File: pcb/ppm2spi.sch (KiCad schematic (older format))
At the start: 38 parts, among them IC1 ATMEGA328-A, K1 CONN_3, P1 CONN_5, P2 CONN_6, P3 CONN_3X2, P4 CONN_6, SW1 SW_PUSH, U1 MCP1702-5v, U2 MCP1702-3.3v, X1 16Mhz

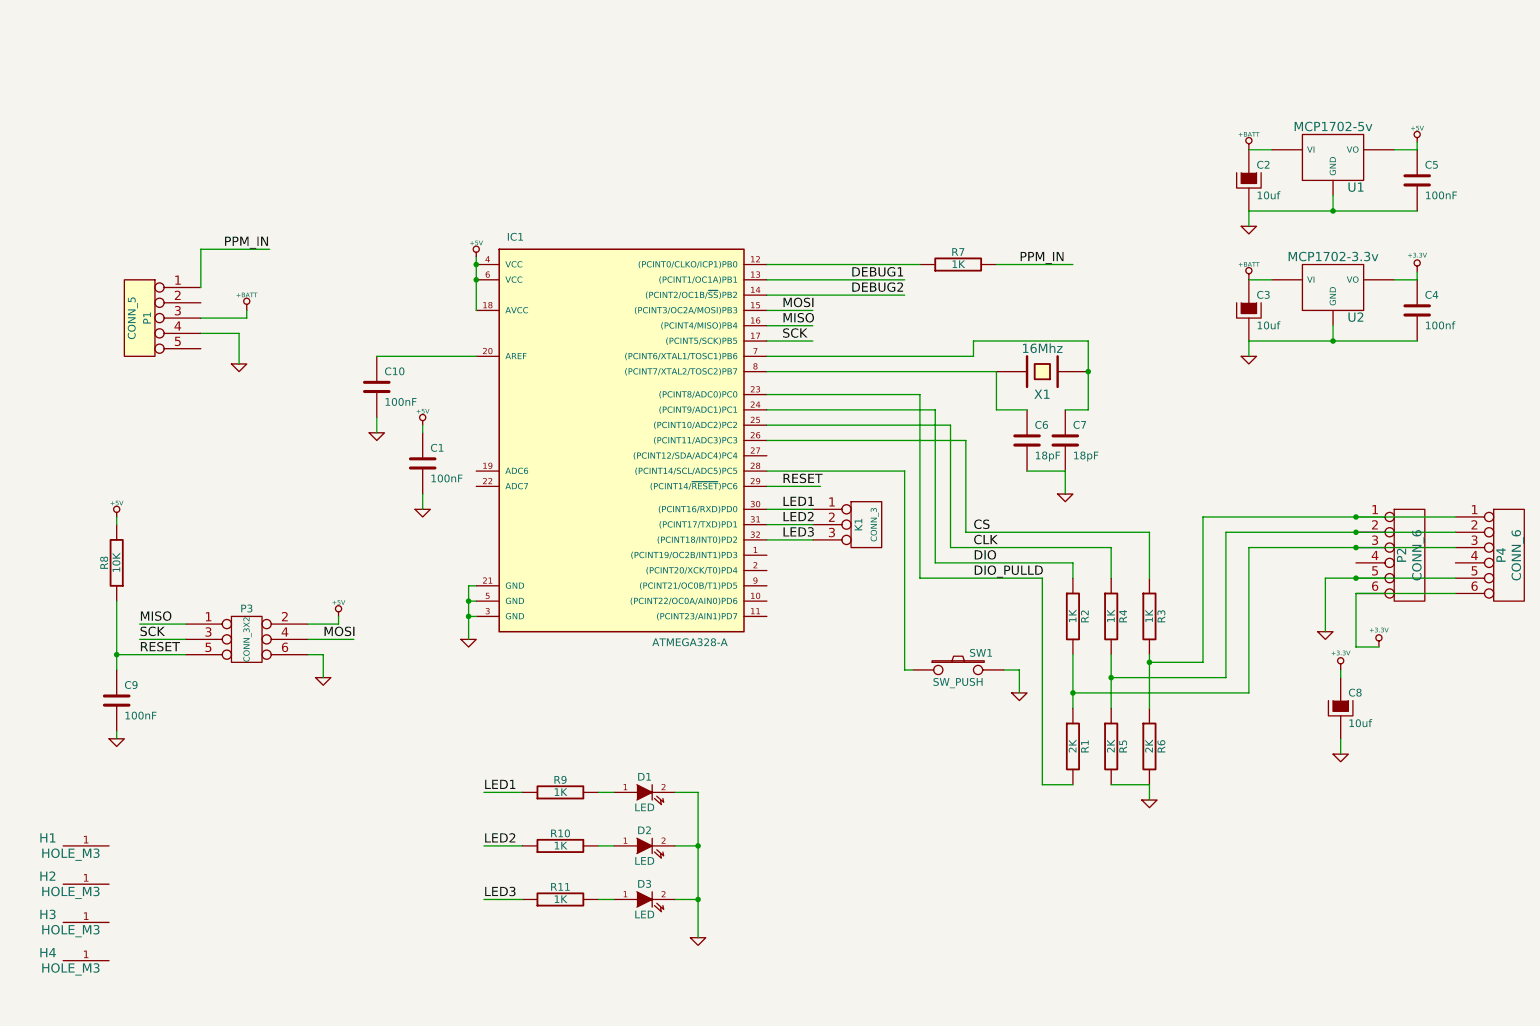
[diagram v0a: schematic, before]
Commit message: Hardware changes to allow a serial input as well as PPM
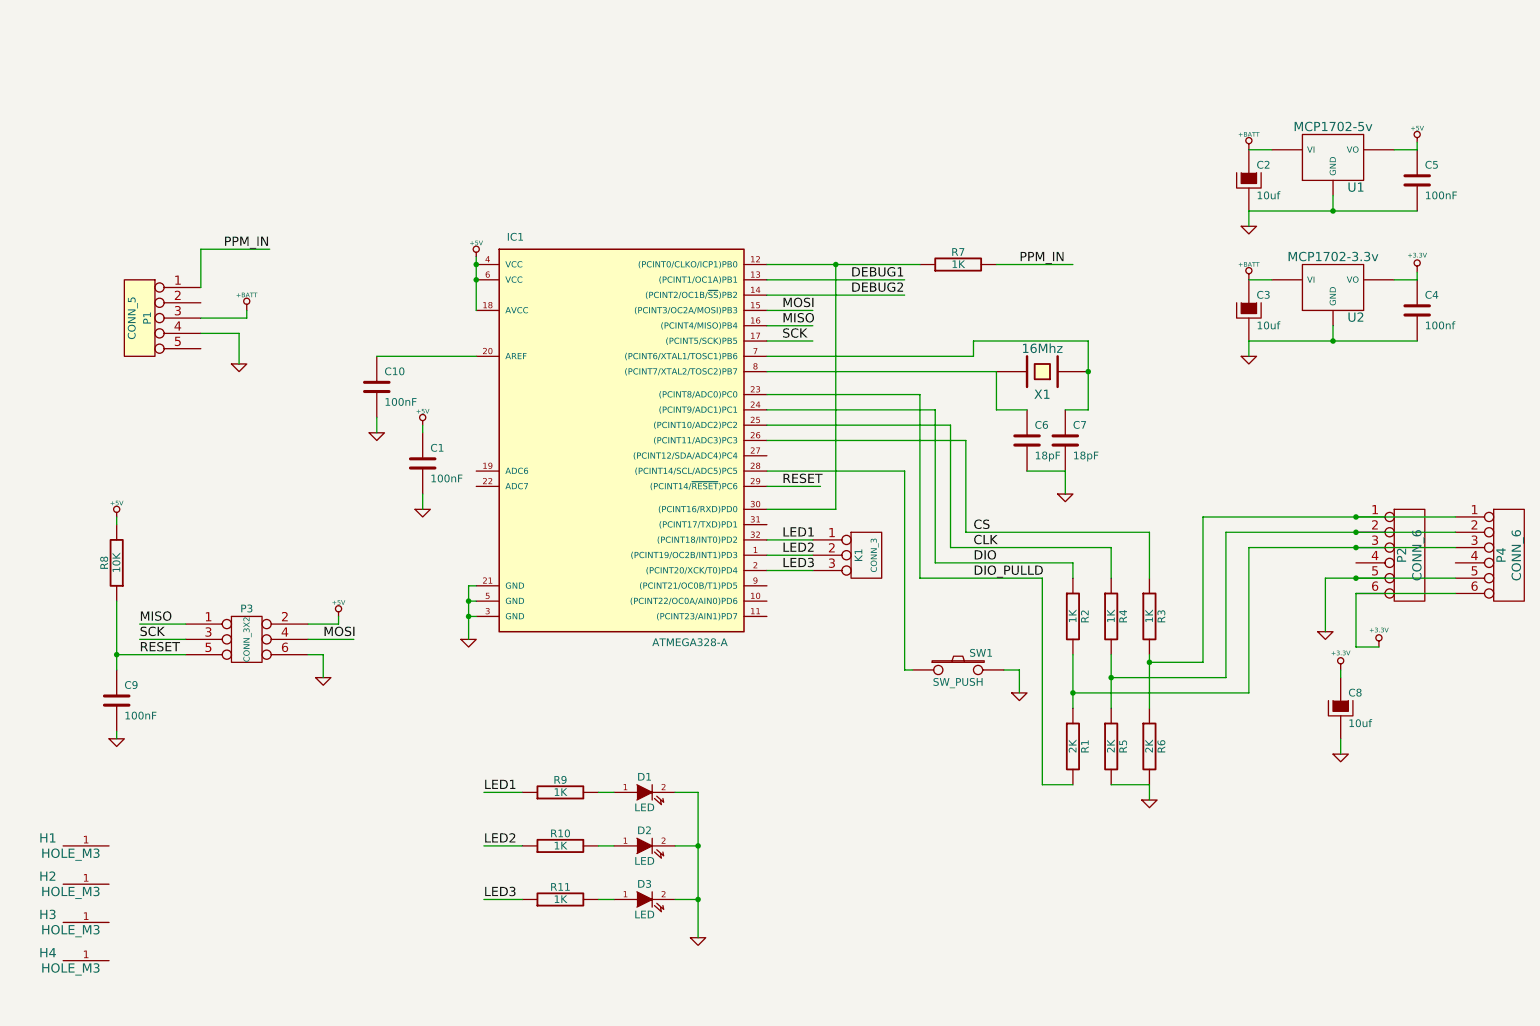
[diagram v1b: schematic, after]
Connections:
- wire segments 112 -> 114
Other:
- moved on the sheet: K1

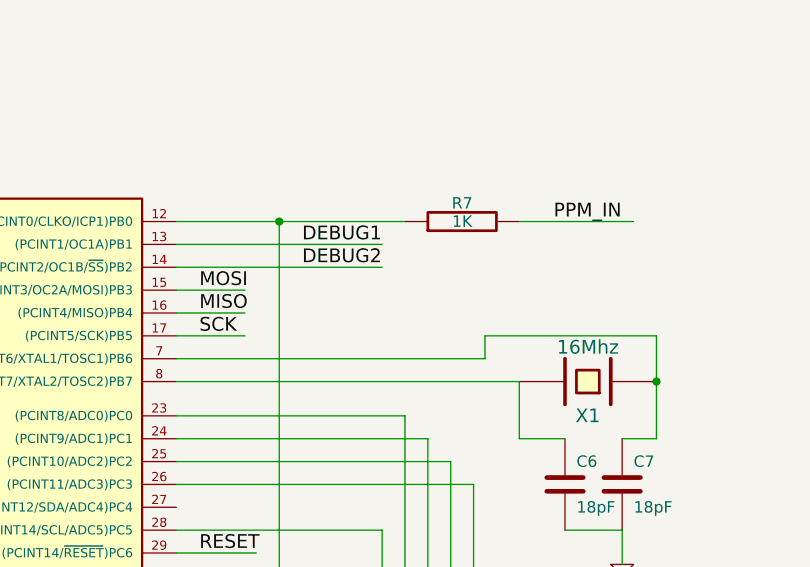
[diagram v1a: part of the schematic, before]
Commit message: Forgot to break out the debug pins
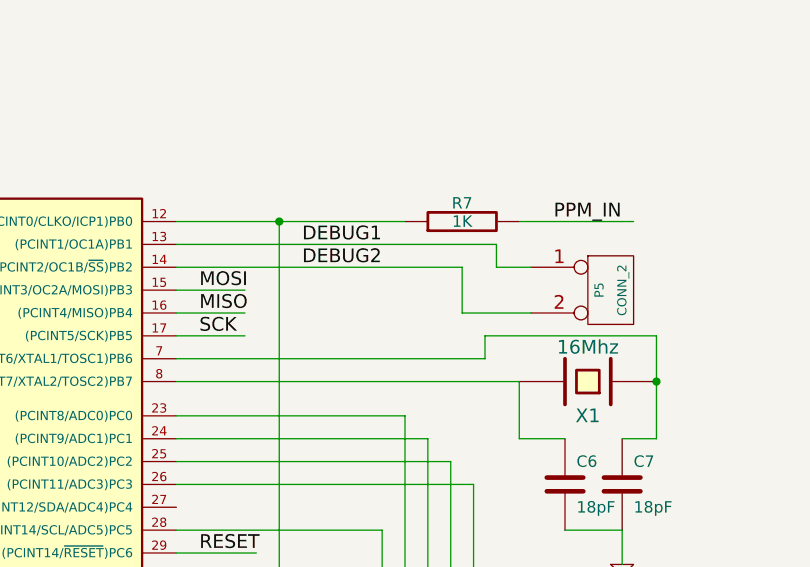
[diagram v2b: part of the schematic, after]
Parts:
- added P5: CONN_2, symbol CONN_2
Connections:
- wire segments 114 -> 118
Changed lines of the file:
@@
-EESchema Schematic File Version 2  date 14/03/2013 13:46:19
+EESchema Schematic File Version 2  date 14/03/2013 13:59:10
 LIBS:power
 LIBS:device
@@
 Comment4 ""
 $EndDescr
+Wire Wire Line
+	7450 2800 7150 2800
+Wire Wire Line
+	7150 2800 7150 2600
+Wire Wire Line
+	7150 2600 5900 2600
 Connection ~ 6350 2400
 Wire Wire Line
@@
 Wire Wire Line
 	5900 3850 6250 3850
-Wire Wire Line
-	6800 2500 5900 2500
 Wire Wire Line
 	5900 3750 6800 3750
@@
 	7400 3100 5900 3100
 Wire Wire Line
-	6800 2600 5900 2600
-Wire Wire Line
 	6900 2400 5900 2400
 Wire Wire Line
@@
 Wire Wire Line
 	6200 4400 5900 4400
+Wire Wire Line
+	5900 2500 7300 2500
+Wire Wire Line
+	7300 2500 7300 2600
+Wire Wire Line
+	7300 2600 7450 2600
+$Comp
+L CONN_2 P5
+U 1 1 5141D78A
+P 7800 2700
+F 0 "P5" V 7750 2700 40  0000 C CNN
+F 1 "CONN_2" V 7850 2700 40  0000 C CNN
+	1    7800 2700
+	1    0    0    -1
+$EndComp
 $Comp
 L CONN_6 P4
@@
 LED1
 $Comp
-L GND #PWR7
+L GND #PWR01
 U 1 1 513E082D
 P 3350 3500
-F 0 "#PWR7" H 3350 3500 30  0001 C CNN
+F 0 "#PWR01" H 3350 3500 30  0001 C CNN
 F 1 "GND" H 3350 3430 30  0001 C CNN
 	1    3350 3500
@@
 $EndComp
 $Comp
-L GND #PWR2
+L GND #PWR02
 U 1 1 513E07C2
 P 1650 5500
-F 0 "#PWR2" H 1650 5500 30  0001 C CNN
+F 0 "#PWR02" H 1650 5500 30  0001 C CNN
 F 1 "GND" H 1650 5430 30  0001 C CNN
 	1    1650 5500
@@
 $EndComp
 $Comp
-L +5V #PWR1
+L +5V #PWR03
 U 1 1 513E07BE
 P 1650 4050
-F 0 "#PWR1" H 1650 4140 20  0001 C CNN
+F 0 "#PWR03" H 1650 4140 20  0001 C CNN
 F 1 "+5V" H 1650 4140 30  0000 C CNN
 	1    1650 4050
@@
 $EndComp
 $Comp
-L +5V #PWR6
+L +5V #PWR04
 U 1 1 513E06E3
 P 3100 4700
-F 0 "#PWR6" H 3100 4790 20  0001 C CNN
+F 0 "#PWR04" H 3100 4790 20  0001 C CNN
 F 1 "+5V" H 3100 4790 30  0000 C CNN
 	1    3100 4700
@@
 $EndComp
 $Comp
-L GND #PWR5
+L GND #PWR05
 U 1 1 513E06E0
 P 3000 5100
-F 0 "#PWR5" H 3000 5100 30  0001 C CNN
+F 0 "#PWR05" H 3000 5100 30  0001 C CNN
 F 1 "GND" H 3000 5030 30  0001 C CNN
 	1    3000 5100
@@
 LED1
 $Comp
-L GND #PWR12
+L GND #PWR06
 U 1 1 513E05CD
 P 5450 6800
-F 0 "#PWR12" H 5450 6800 30  0001 C CNN
+F 0 "#PWR06" H 5450 6800 30  0001 C CNN
 F 1 "GND" H 5450 6730 30  0001 C CNN
 	1    5450 6800
@@
 $EndComp
 $Comp
-L GND #PWR9
+L GND #PWR07
 U 1 1 513E05A6
 P 3650 4000
-F 0 "#PWR9" H 3650 4000 30  0001 C CNN
+F 0 "#PWR07" H 3650 4000 30  0001 C CNN
 F 1 "GND" H 3650 3930 30  0001 C CNN
 	1    3650 4000
@@
 $EndComp
 $Comp
-L +5V #PWR8
+L +5V #PWR08
 U 1 1 513E05A3
 P 3650 3450
-F 0 "#PWR8" H 3650 3540 20  0001 C CNN
+F 0 "#PWR08" H 3650 3540 20  0001 C CNN
 F 1 "+5V" H 3650 3540 30  0000 C CNN
 	1    3650 3450
@@
 PPM_IN
 $Comp
-L GND #PWR13
+L GND #PWR09
 U 1 1 513E054D
 P 7550 5200
-F 0 "#PWR13" H 7550 5200 30  0001 C CNN
+F 0 "#PWR09" H 7550 5200 30  0001 C CNN
 F 1 "GND" H 7550 5130 30  0001 C CNN
 	1    7550 5200
@@
 $EndComp
 $Comp
-L +3.3V #PWR21
+L +3.3V #PWR010
 U 1 1 513E04F8
 P 9650 5050
-F 0 "#PWR21" H 9650 5010 30  0001 C CNN
+F 0 "#PWR010" H 9650 5010 30  0001 C CNN
 F 1 "+3.3V" H 9650 5160 30  0000 C CNN
 	1    9650 5050
@@
 $EndComp
 $Comp
-L GND #PWR22
+L GND #PWR011
 U 1 1 513E04F3
 P 9650 5600
-F 0 "#PWR22" H 9650 5600 30  0001 C CNN
+F 0 "#PWR011" H 9650 5600 30  0001 C CNN
 F 1 "GND" H 9650 5530 30  0001 C CNN
 	1    9650 5600
@@
 $EndComp
 $Comp
-L +3.3V #PWR23
+L +3.3V #PWR012
 U 1 1 513E04BE
 P 9900 4900
-F 0 "#PWR23" H 9900 4860 30  0001 C CNN
+F 0 "#PWR012" H 9900 4860 30  0001 C CNN
 F 1 "+3.3V" H 9900 5010 30  0000 C CNN
 	1    9900 4900
@@
 $EndComp
 $Comp
-L GND #PWR20
+L GND #PWR013
 U 1 1 513E04B0
 P 9550 4800
-F 0 "#PWR20" H 9550 4800 30  0001 C CNN
+F 0 "#PWR013" H 9550 4800 30  0001 C CNN
 F 1 "GND" H 9550 4730 30  0001 C CNN
 	1    9550 4800
@@
 $EndComp
 $Comp
-L +5V #PWR11
+L +5V #PWR014
 U 1 1 513E045A
 P 4000 2350
-F 0 "#PWR11" H 4000 2440 20  0001 C CNN
+F 0 "#PWR014" H 4000 2440 20  0001 C CNN
 F 1 "+5V" H 4000 2440 30  0000 C CNN
 	1    4000 2350
@@
 $EndComp
 $Comp
-L GND #PWR10
+L GND #PWR015
 U 1 1 513E0448
 P 3950 4850
-F 0 "#PWR10" H 3950 4850 30  0001 C CNN
+F 0 "#PWR015" H 3950 4850 30  0001 C CNN
 F 1 "GND" H 3950 4780 30  0001 C CNN
 	1    3950 4850
@@
 CS
 $Comp
-L GND #PWR15
+L GND #PWR016
 U 1 1 513E0385
 P 8400 5900
-F 0 "#PWR15" H 8400 5900 30  0001 C CNN
+F 0 "#PWR016" H 8400 5900 30  0001 C CNN
 F 1 "GND" H 8400 5830 30  0001 C CNN
 	1    8400 5900
@@
 $EndComp
 $Comp
-L +3.3V #PWR25
+L +3.3V #PWR017
 U 1 1 513E027A
 P 10150 2450
-F 0 "#PWR25" H 10150 2410 30  0001 C CNN
+F 0 "#PWR017" H 10150 2410 30  0001 C CNN
 F 1 "+3.3V" H 10150 2560 30  0000 C CNN
 	1    10150 2450
@@
 $EndComp
 $Comp
-L +5V #PWR24
+L +5V #PWR018
 U 1 1 513E0273
 P 10150 1600
-F 0 "#PWR24" H 10150 1690 20  0001 C CNN
+F 0 "#PWR018" H 10150 1690 20  0001 C CNN
 F 1 "+5V" H 10150 1690 30  0000 C CNN
 	1    10150 1600
@@
 $EndComp
 $Comp
-L +BATT #PWR4
+L +BATT #PWR019
 U 1 1 513E01EB
 P 2500 2700
-F 0 "#PWR4" H 2500 2650 20  0001 C CNN
+F 0 "#PWR019" H 2500 2650 20  0001 C CNN
 F 1 "+BATT" H 2500 2800 30  0000 C CNN
 	1    2500 2700
@@
 $EndComp
 $Comp
-L +BATT #PWR18
+L +BATT #PWR020
 U 1 1 513E01E7
 P 9050 2500
-F 0 "#PWR18" H 9050 2450 20  0001 C CNN
+F 0 "#PWR020" H 9050 2450 20  0001 C CNN
 F 1 "+BATT" H 9050 2600 30  0000 C CNN
 	1    9050 2500
@@
 $EndComp
 $Comp
-L +BATT #PWR16
+L +BATT #PWR021
 U 1 1 513E01E0
 P 9050 1650
-F 0 "#PWR16" H 9050 1600 20  0001 C CNN
+F 0 "#PWR021" H 9050 1600 20  0001 C CNN
 F 1 "+BATT" H 9050 1750 30  0000 C CNN
 	1    9050 1650
@@
 PPM_IN
 $Comp
-L GND #PWR3
+L GND #PWR022
 U 1 1 513E01B7
 P 2450 3050
-F 0 "#PWR3" H 2450 3050 30  0001 C CNN
+F 0 "#PWR022" H 2450 3050 30  0001 C CNN
 F 1 "GND" H 2450 2980 30  0001 C CNN
 	1    2450 3050
@@
 $EndComp
 $Comp
-L GND #PWR17
+L GND #PWR023
 U 1 1 513E019B
 P 9050 2150
-F 0 "#PWR17" H 9050 2150 30  0001 C CNN
+F 0 "#PWR023" H 9050 2150 30  0001 C CNN
 F 1 "GND" H 9050 2080 30  0001 C CNN
 	1    9050 2150
@@
 $EndComp
 $Comp
-L GND #PWR19
+L GND #PWR024
 U 1 1 513E0198
 P 9050 3000
-F 0 "#PWR19" H 9050 3000 30  0001 C CNN
+F 0 "#PWR024" H 9050 3000 30  0001 C CNN
 F 1 "GND" H 9050 2930 30  0001 C CNN
 	1    9050 3000
@@
 $EndComp
 $Comp
-L GND #PWR14
+L GND #PWR025
 U 1 1 513E0151
 P 7850 3900
-F 0 "#PWR14" H 7850 3900 30  0001 C CNN
+F 0 "#PWR025" H 7850 3900 30  0001 C CNN
 F 1 "GND" H 7850 3830 30  0001 C CNN
 	1    7850 3900

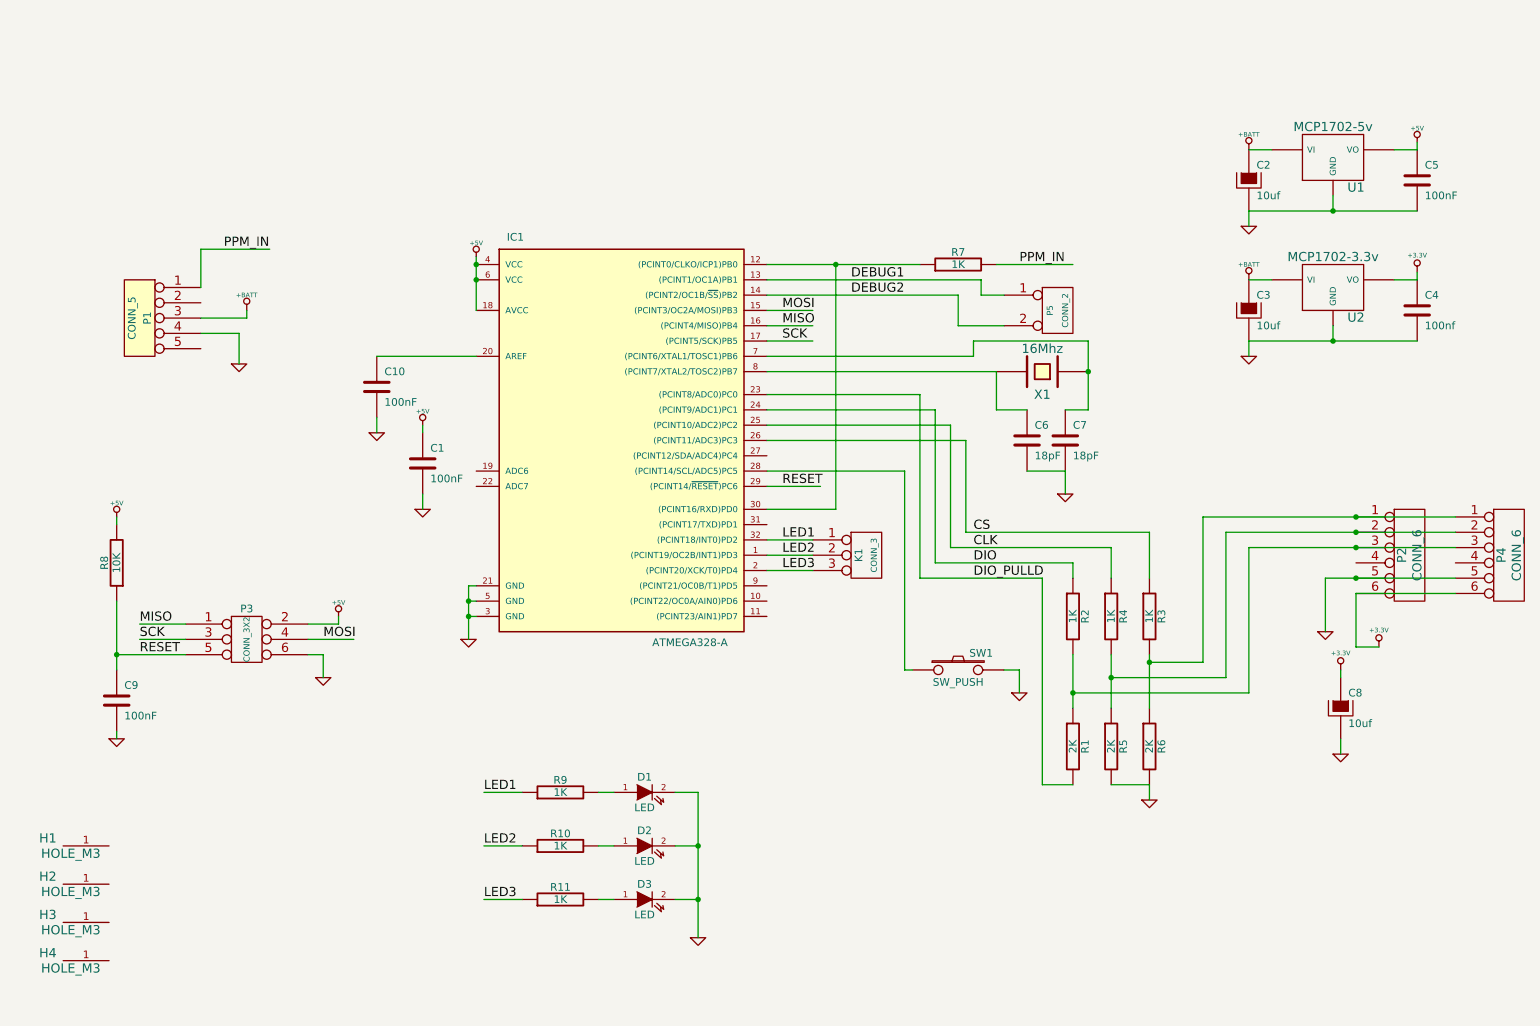
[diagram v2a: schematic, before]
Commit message: Update to hardware SPI, schematic also changed. PCB needs redoing. Notes added to schematic to make it easier to understand.
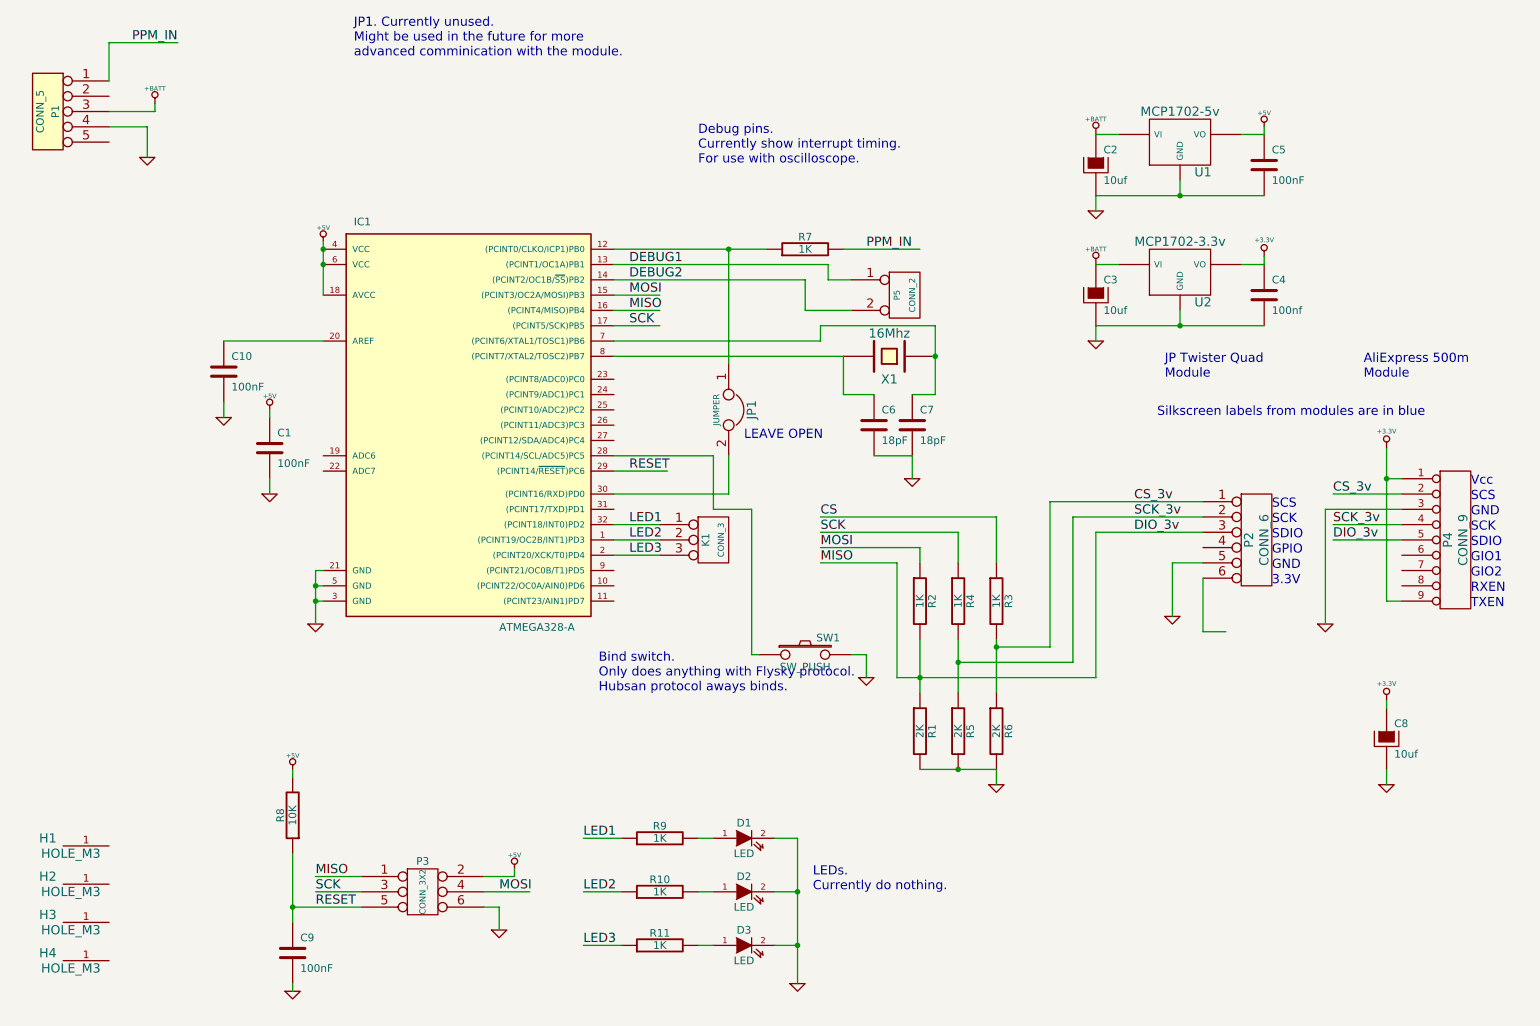
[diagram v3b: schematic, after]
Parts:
- removed P4: CONN_6, symbol CONN_6
- added JP1: JUMPER, ~, symbol JUMPER
- added P4: CONN_9, symbol CONN_9
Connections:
- net labels added: CS_3v, DIO_3v, SCK_3v
- net labels removed: CLK, DIO, DIO_PULLD
- wire segments 118 -> 119
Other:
- note added: "3.3V"
- note added: "AliExpress 500m\nModule"
- note added: "Bind switch.\nOnly does anything with Flysky protocol.\nHubsan protocol aways binds."
- note added: "Debug pins.\nCurrently show interrupt timing.\nFor use with oscilloscope."
- note added: "GIO1"
- note added: "GIO2"
- note added: "GND"
- note added: "GPIO"
- note added: "JP Twister Quad\nModule"
- note added: "JP1. Currently unused.\nMight be used in the future for more\nadvanced comminication with the module."
- note added: "LEAVE OPEN"
- note added: "LEDs.\nCurrently do nothing."
- note added: "RXEN"
- note added: "SCK"
- note added: "SCS"
- note added: "SDIO"
- note added: "Silkscreen labels from modules are in blue"
- note added: "TXEN"
- note added: "Vcc"
- moved on the sheet: C1, C10, C2, C3, C4, C5, C6, C7, C8, C9, D1, D2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
